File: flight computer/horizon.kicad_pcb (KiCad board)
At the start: 4 copper layers, 50.8 x 95.7 mm, 46 parts, among them J10 Conn_01x02_Pin, J11 USB_C_Receptacle_USB2.0_16P, J12 Conn_01x04, J13 1x3 servo, J14 1x3 servo, J15 arming terminal, J16 arming terminal, J18 Conn_02x03_Counter_Clockwise, J19 Screw_Terminal_01x02, J20 Screw_Terminal_01x02, J21 Conn_02x03_Counter_Clockwise, J5 Screw_Term, J6 1x3 servo, J9 1x3 servo, Q2 DMG2301L, U1 MMCU, U13 LTC4412xS6, U15 AP2112K-3.3, U3 TPS61200DRC, U9 TPS82130

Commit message: chips yummy
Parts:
- added C10: 12pF, Capacitor_SMD:C_0603_1608Metric, B.Cu at (184.1, 55.8)
- added C11: 100nF, Capacitor_SMD:C_0603_1608Metric, F.Cu at (317.2, 42.3)
- added C12: 1uF, Capacitor_SMD:C_0603_1608Metric, F.Cu at (317.2, 44.9)
- added C13: 100nF, Capacitor_SMD:C_0603_1608Metric, F.Cu at (317.2, 47.4)
- added C16: 4n7, Capacitor_SMD:C_0603_1608Metric, F.Cu at (157.7, 28.9)
- added C17: 12pF, Capacitor_SMD:C_0603_1608Metric, B.Cu at (188.0, 52.5)
- added C27: 100n, Capacitor_SMD:C_0603_1608Metric, F.Cu at (157.7, 31.4)
- added C5: 100nF, Capacitor_SMD:C_0603_1608Metric, B.Cu at (186.7, 40.1)
- added C6: 100nF, Capacitor_SMD:C_0603_1608Metric, B.Cu at (185.4, 51.9)
- added C63: 1uF, Capacitor_SMD:C_0603_1608Metric, B.Cu at (187.3, 65.0)
- added C64: 0.1uF, Capacitor_SMD:C_0603_1608Metric, B.Cu at (189.4, 67.1)
- added C65: 0.1uF, Capacitor_SMD:C_0603_1608Metric, B.Cu at (185.9, 63.4)
- added C66: 0.1uF, Capacitor_SMD:C_0603_1608Metric, B.Cu at (184.8, 62.4)
- added C67: 4.7uF, Capacitor_SMD:C_0603_1608Metric, B.Cu at (188.4, 66.0)
- added C7: 100nF, Capacitor_SMD:C_0603_1608Metric, B.Cu at (176.8, 49.2)
- added C72: 1uF, Capacitor_SMD:C_0603_1608Metric, B.Cu at (177.9, 50.3)
- added C77: 100nF, Capacitor_SMD:C_0603_1608Metric, B.Cu at (177.9, 40.4)
- added C78: 100nF, Capacitor_SMD:C_0603_1608Metric, F.Cu at (321.2, 47.4)
- added C79: 100nF, Capacitor_SMD:C_0603_1608Metric, B.Cu at (176.9, 41.4)
- added C8: 100nF, Capacitor_SMD:C_0603_1608Metric, F.Cu at (317.2, 34.8)
- added C9: 100nF, Capacitor_SMD:C_0603_1608Metric, F.Cu at (317.2, 37.3)
- added D7: LED, LED_SMD:LED_0603_1608Metric, F.Cu at (161.8, 28.9)
- added R10: 2.2k, Resistor_SMD:R_0603_1608Metric, B.Cu at (176.4, 58.0)
- added R13: 2.2k, Resistor_SMD:R_0603_1608Metric, B.Cu at (176.4, 60.5)
- added R14: 1.5k, Resistor_SMD:R_0603_1608Metric, F.Cu at (329.3, 27.3)
- added R20: 5k1, Resistor_SMD:R_0603_1608Metric, B.Cu at (198.5, 33.5)
- added R21: 5k1, Resistor_SMD:R_0603_1608Metric, B.Cu at (201.4, 33.5)
- added R22: 330, Resistor_SMD:R_0603_1608Metric, F.Cu at (157.7, 38.9)
- added R26: 2.2K, Resistor_SMD:R_0603_1608Metric, F.Cu at (329.3, 29.8)
- added R29: 2.2K, Resistor_SMD:R_0603_1608Metric, B.Cu at (199.6, 53.5)
- added R30: 2.2K, Resistor_SMD:R_0603_1608Metric, B.Cu at (200.7, 54.6)
- added R6: 4.7k, Resistor_SMD:R_0603_1608Metric, B.Cu at (200.1, 64.0)
- added R7: 4.7k, Resistor_SMD:R_0603_1608Metric, B.Cu at (199.0, 65.1)
- added R9: 1.5k, Resistor_SMD:R_0603_1608Metric, B.Cu at (186.5, 50.8)
- added Y1: Crystal, Crystal:Crystal_AT310_D3.0mm_L10.0mm_Vertical, F.Cu at (187.3, 54.4)
- moved J21 15.3 mm to (192.5, 30.2), turned to 180 degrees
- moved J18 15.1 mm to (206.9, 25.1), turned to 0 degrees
- moved D8 1.83 mm to (199.8, 36.8), turned to -45 degrees
- turned SAMD21G18A-AU1 to -45 degrees
- turned SAMD21G18A-AU2 to -135 degrees
- turned U1 to 45 degrees
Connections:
- J18 pad 2: D+ DMCU-1 -> D+ DMCU-2
- J18 pad 4: unconnected-(J18-Pin_4-Pad4) -> D+ MMCU
- J18 pad 6: D+ DMCU-2 -> D+ DMCU-1
- J21 pad 2: D- DMCU-1 -> D- DMCU-2
- J21 pad 6: D- DMCU-2 -> D- DMCU-1
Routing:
- net I2C0_SDA: track 0.00 -> 24.4 mm, vias 0 -> 2
- net D+: track 0.00 -> 21.4 mm
- net I2C0_SCL: track 0.00 -> 21.4 mm
- net D-: track 0.00 -> 20.3 mm
- net Net-(D26-A): track 0.00 -> 11.0 mm, vias 0 -> 1
- net Net-(U1-XTAL32): track 0.00 -> 4.10 mm
- net Net-(U1-EXTAL32): track 0.00 -> 3.77 mm
- net Net-(J11-CC2): track 0.00 -> 1.84 mm
- net Net-(J11-CC1): track 0.00 -> 1.81 mm
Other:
- board text removed: "WORK ON THIS ONE... the top is a working version of it, so pretty much take our parts, and put them in the some pos if you can, and wire it to the MCU were needed normally. Also, keep it in the same spot as the RF use to be."

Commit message: more wiring fuck this
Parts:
- C11, C12, C13, C78, C8, C9, R14, R26: moved to B.Cu
- moved R14 132.7 mm to (198.4, 49.2), turned to -135 degrees
- moved R26 124.8 mm to (206.5, 52.4), turned to -45 degrees
- moved C9 120.6 mm to (197.0, 47.7), turned to 45 degrees
- moved C12 118.8 mm to (198.5, 41.2), turned to -45 degrees
- moved C8 117.7 mm to (199.6, 40.2), turned to -45 degrees
- moved C78 113.6 mm to (207.9, 39.6), turned to -135 degrees
- moved C13 108.5 mm to (209.0, 40.7), turned to -135 degrees
- moved C11 108.1 mm to (209.4, 49.6), turned to 135 degrees
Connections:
- J18 pad 2: D+ DMCU-2 -> D+ DMCU-1
- J18 pad 6: D+ DMCU-1 -> D+ DMCU-2
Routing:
- net D+ MMCU: track 0.00 -> 48.1 mm
- net D+ DMCU-1: track 0.00 -> 39.2 mm
- net D- MMCU: track 0.00 -> 37.9 mm, vias 0 -> 2
- net D- DMCU-1: track 0.00 -> 28.2 mm
- net D- DMCU-2: track 0.00 -> 23.4 mm, vias 0 -> 2
- net D+ DMCU-2: track 0.00 -> 21.0 mm

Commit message: finished basics, proof check time
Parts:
- C16, C27, D7, R22: moved to B.Cu
- moved C16 46.3 mm to (203.8, 32.8), turned to 180 degrees
- moved C27 46.2 mm to (203.8, 34.4), turned to 180 degrees
- moved R22 46.0 mm to (203.6, 35.9), turned to 180 degrees
- moved D7 45.2 mm to (206.8, 33.5), turned to -120 degrees
- moved R13 17.7 mm to (189.2, 48.2), turned to 0 degrees
- moved R10 15.2 mm to (189.7, 50.6), turned to -30 degrees
- moved C77 0.19 mm to (177.9, 40.2)
- moved C79 0.19 mm to (176.8, 41.3)
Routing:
- net +5V: track 1.91 -> 56.2 mm
- net GND: track 10.8 -> 59.6 mm, vias 9 -> 42
- net SERVO1: track 0.00 -> 43.2 mm, vias 0 -> 1
- net +3.3V: track 3.26 -> 42.2 mm, vias 0 -> 13
- net SERVO2: track 0.00 -> 38.2 mm, vias 0 -> 1
- net CAM_TX: track 0.00 -> 26.6 mm, vias 0 -> 1
- net CAM_RX: track 0.00 -> 24.6 mm, vias 0 -> 1
- net PTD4: track 0.00 -> 23.6 mm, vias 0 -> 2
- net SERVO3: track 0.00 -> 15.5 mm
- net PTA12: track 0.00 -> 15.4 mm, vias 0 -> 2
- net SERVO4: track 0.00 -> 11.0 mm
- net SERVO5: track 0.00 -> 9.93 mm
- net StatusLED_3: track 0.00 -> 5.03 mm, vias 0 -> 1
- net D+ DMCU-1: track 39.2 -> 42.3 mm
- net Net-(D7-A): track 0.00 -> 2.68 mm
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
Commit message: more wiring kms
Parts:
- added D3: LED, LED_SMD:LED_0603_1608Metric, F.Cu at (177.7, 37.0)
- added D4: LED, LED_SMD:LED_0603_1608Metric, F.Cu at (209.7, 36.1)
- added F1: Polyfuse, Fuse:Fuse_0603_1608Metric, F.Cu at (174.4, 32.8)
- added F2: Polyfuse, Fuse:Fuse_0603_1608Metric, F.Cu at (212.8, 30.3)
- added Q1: IRLML6402, Package_TO_SOT_SMD:SOT-23, F.Cu at (143.4, 72.9)
- added Q3: IRLML6402, Package_TO_SOT_SMD:SOT-23, F.Cu at (143.4, 77.5)
- added Q4: IRLML6402, Package_TO_SOT_SMD:SOT-23, F.Cu at (148.3, 72.9)
- added Q5: IRLML6402, Package_TO_SOT_SMD:SOT-23, F.Cu at (148.3, 77.5)
- added Q6: IRLML6402, Package_TO_SOT_SMD:SOT-23, F.Cu at (153.2, 72.9)
- added Q8: IRLML6402, Package_TO_SOT_SMD:SOT-23, F.Cu at (174.4, 35.8)
- added Q9: IRLML6402, Package_TO_SOT_SMD:SOT-23, F.Cu at (212.2, 35.6)
- added R58: 1k, Resistor_SMD:R_0603_1608Metric, F.Cu at (177.2, 38.5)
- added R59: 1k, Resistor_SMD:R_0603_1608Metric, F.Cu at (209.2, 38.3)
- added R62: 100k, Resistor_SMD:R_0603_1608Metric, F.Cu at (159.0, 61.7)
- added R63: 100, Resistor_SMD:R_0603_1608Metric, F.Cu at (159.0, 64.2)
- added R64: 100, Resistor_SMD:R_0603_1608Metric, F.Cu at (159.0, 66.8)
- added R65: 100, Resistor_SMD:R_0603_1608Metric, F.Cu at (159.0, 69.3)
- added R66: 100, Resistor_SMD:R_0603_1608Metric, F.Cu at (163.0, 46.7)
- added R67: 100, Resistor_SMD:R_0603_1608Metric, F.Cu at (163.0, 49.2)
- added R68: 100k, Resistor_SMD:R_0603_1608Metric, F.Cu at (163.0, 51.7)
- added R69: 100k, Resistor_SMD:R_0603_1608Metric, F.Cu at (163.0, 54.2)
- added R70: 100k, Resistor_SMD:R_0603_1608Metric, F.Cu at (163.0, 56.7)
- added R71: 100k, Resistor_SMD:R_0603_1608Metric, F.Cu at (163.0, 59.2)
- added R78: 10k, Resistor_SMD:R_0603_1608Metric, F.Cu at (174.2, 38.5)
- added R79: 100, Resistor_SMD:R_0603_1608Metric, F.Cu at (180.3, 35.4)
- added R80: 10k, Resistor_SMD:R_0603_1608Metric, F.Cu at (212.2, 38.3)
- added R81: 100, Resistor_SMD:R_0603_1608Metric, F.Cu at (212.0, 32.8)
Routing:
- net mosfet2_signalfire: track 0.00 -> 33.9 mm, vias 0 -> 3
- net +5V: track 56.2 -> 79.6 mm
- net mosfet1_signalfire: track 0.00 -> 8.40 mm, vias 0 -> 1
- net Net-(D3-K): track 0.00 -> 6.41 mm
- net Net-(D4-K): track 0.00 -> 6.08 mm
- net Net-(Q8-G): track 0.00 -> 4.33 mm
- net Net-(Q9-D): track 0.00 -> 3.76 mm
- net Net-(Q8-D): track 0.00 -> 3.70 mm
- net GND: track 59.6 -> 63.2 mm, vias 42 -> 43
- net Net-(J20-Pin_1): track 0.00 -> 2.39 mm
- net Net-(SAMD21G18A-AU2-GNDANA): track 0.00 -> 2.01 mm
- net Net-(Q9-G): track 0.00 -> 1.99 mm
- net Net-(J15-Pin_2): track 0.00 -> 1.86 mm
- net Net-(D3-A): track 0.00 -> 1.77 mm

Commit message: wiring fml
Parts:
- removed Q1, Q3, Q4, Q5, Q6: IRLML6402, Package_TO_SOT_SMD:SOT-23
- removed R62, R68, R69, R70, R71: 100k, Resistor_SMD:R_0603_1608Metric
- removed R63, R64, R65, R66, R67: 100, Resistor_SMD:R_0603_1608Metric
- added SW1: CK_KMS2xxG, Button_Switch_SMD:SW_SPST_CK_KMS2xxGP, B.Cu at (169.9, 62.9)
- added U2: MKL02Z32VFG4, Package_DFN_QFN:QFN-16-1EP_3x3mm_P0.5mm_EP1.9x1.9mm, B.Cu at (181.4, 54.0)
- moved C10 0.31 mm to (184.4, 55.7)
- moved Y1 0.11 mm to (187.3, 54.5)
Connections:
- 1x3servo1 pad 2: Net-(1x3servo1-Pin_2) -> +5V
- F2 pad 1: Net-(J20-Pin_1) -> unconnected-(F2-Pad1)
- J13 pad 2: Net-(J13-Pin_2) -> +5V
- J14 pad 2: Net-(J14-Pin_2) -> +5V
- J20 pad 1: Net-(J20-Pin_1) -> unconnected-(J20-Pin_1-Pad1)
- J20 pad 2: Net-(D4-K) -> unconnected-(J20-Pin_2-Pad2)
- J5 pad 1: Net-(IC1-OUT1) -> unconnected-(J5-Pin_1-Pad1)
- J5 pad 2: Net-(IC1-OUT2) -> unconnected-(J5-Pin_2-Pad2)
- J6 pad 2: Net-(J6-Pin_2) -> +5V
- J9 pad 2: Net-(J9-Pin_2) -> +5V
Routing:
- net +5V: track 79.6 -> 121.5 mm
- net nRESET MMCU: track 0.00 -> 27.4 mm, vias 0 -> 2
- net Net-(U2-PTB2/IRQ_7): track 0.00 -> 17.8 mm
- net SWCLK MMCU: track 0.00 -> 16.0 mm, vias 0 -> 4
- net PTA3: track 0.00 -> 15.8 mm, vias 0 -> 2
- net SWDIO MMCU: track 0.00 -> 14.3 mm, vias 0 -> 2
- net PTA2: track 0.00 -> 10.4 mm, vias 0 -> 4
- net GND: track 63.2 -> 68.6 mm, vias 43 -> 47
- net Net-(J20-Pin_1): track 2.39 -> 0.00 mm
- net (no net): track 0.00 -> 2.39 mm
- net +3.3V: track 42.2 -> 43.7 mm, vias 13 -> 14
- net Net-(U1-XTAL32): track 4.10 -> 5.21 mm
- net D+ DMCU-1: track 42.3 -> 41.4 mm, vias 0 -> 2
- net D- MMCU: track 37.9 -> 38.7 mm

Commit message: i did stuffs
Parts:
- added C1: 100 nF, Capacitor_SMD:C_0603_1608Metric, F.Cu at (69.2, 9.72)
- added C14: 8pF, Capacitor_SMD:C_0603_1608Metric, F.Cu at (69.2, 19.8)
- added C15: 100nF, Capacitor_SMD:C_0603_1608Metric, B.Cu at (198.6, 113.0)
- added C18: 4.7uF, Capacitor_SMD:C_0603_1608Metric, F.Cu at (69.2, 24.8)
- added C19: 100nF, Capacitor_SMD:C_0603_1608Metric, F.Cu at (69.2, 27.3)
- added C2: 100 nF, Capacitor_SMD:C_0603_1608Metric, F.Cu at (69.2, 12.2)
- added C20: 100nF, Capacitor_SMD:C_0603_1608Metric, F.Cu at (73.2, 9.72)
- added C3: 100 nF, Capacitor_SMD:C_0603_1608Metric, F.Cu at (69.2, 14.7)
- added C37: 100nF, Capacitor_SMD:C_0603_1608Metric, F.Cu at (73.2, 12.2)
- added C38: 100nF, Capacitor_SMD:C_0603_1608Metric, F.Cu at (73.2, 14.7)
- added C39: 8pF, Capacitor_SMD:C_0603_1608Metric, F.Cu at (73.2, 17.3)
- added C4: 1.2 pF, Capacitor_SMD:C_0603_1608Metric, F.Cu at (69.2, 17.3)
- added C40: 470nF, Capacitor_SMD:C_0603_1608Metric, F.Cu at (73.2, 19.8)
- added C44: 100nF, Capacitor_SMD:C_0603_1608Metric, F.Cu at (73.2, 22.3)
- added C45: 100nF, Capacitor_SMD:C_0603_1608Metric, F.Cu at (73.2, 24.8)
- added C46: 1nF, Capacitor_SMD:C_0603_1608Metric, F.Cu at (73.2, 27.3)
- added C47: 47nF, Capacitor_SMD:C_0603_1608Metric, F.Cu at (77.2, 9.72)
- added C48: 47pF, Capacitor_SMD:C_0603_1608Metric, F.Cu at (77.2, 12.2)
- added C49: 100pF, Capacitor_SMD:C_0603_1608Metric, F.Cu at (77.2, 14.7)
- added C50: 100nF, Capacitor_SMD:C_0603_1608Metric, F.Cu at (77.2, 17.3)
- added C51: 100nF, Capacitor_SMD:C_0603_1608Metric, F.Cu at (77.2, 19.8)
- added D1: D_Schottky, Diode_SMD:D_0603_1608Metric, F.Cu at (102.1, 36.7)
- added D2: PESD5V‑S5ULC, Diode_SMD:D_0603_1608Metric, F.Cu at (102.1, 39.3)
- added FL1: 0900FM15K0039, RF_Converter:Balun_Johanson_0900FM15K0039, F.Cu at (105.9, 37.6)
- added J1: Micro_SD_Card_Det1, Connector_Card:microSD_HC_Hirose_DM3D-SF, F.Cu at (174.5, 111.5)
- added J17: H9161TR-ND, U.FL-R-SMT_01_:HRS_U.FL-R-SMT_01_, F.Cu at (84.9, 40.8)
- added J2: Conn_02x03_Counter_Clockwise, Connector_PinHeader_2.54mm:PinHeader_2x03_P2.54mm_Vertical, F.Cu at (112.1, 10.8)
- added J3: H9161TR-ND, U.FL-R-SMT_01_:HRS_U.FL-R-SMT_01_, F.Cu at (84.9, 30.7)
- added J4: H9161TR-ND, U.FL-R-SMT_01_:HRS_U.FL-R-SMT_01_, F.Cu at (84.9, 35.7)
- added J7: Conn_02x03_Counter_Clockwise, Connector_PinHeader_2.54mm:PinHeader_2x03_P2.54mm_Vertical, F.Cu at (119.3, 10.8)
- added J8: Conn_02x03_Counter_Clockwise, Connector_PinHeader_2.54mm:PinHeader_2x03_P2.54mm_Vertical, F.Cu at (126.5, 10.8)
- added L1: 47 nH, Inductor_SMD:L_0603_1608Metric, F.Cu at (77.2, 22.3)
- added L10: 47nH, Inductor_SMD:L_0603_1608Metric, F.Cu at (77.2, 27.3)
- added L11: 15uH, Inductor_SMD:L_0805_2012Metric, F.Cu at (102.4, 46.6)
- added L3: 3.9 nH, Inductor_SMD:L_0603_1608Metric, F.Cu at (77.2, 24.8)
- added Q7: BSS138, Package_TO_SOT_SMD:SOT-23, F.Cu at (102.5, 43.0)
- added R1: 10 kΩ, Resistor_SMD:R_0603_1608Metric, F.Cu at (81.3, 9.72)
- added R11: 10kΩ, Resistor_SMD:R_0603_1608Metric, F.Cu at (81.3, 17.3)
- added R12: 10kΩ, Resistor_SMD:R_0603_1608Metric, B.Cu at (176.0, 106.1)
- added R2: 10 kΩ, Resistor_SMD:R_0603_1608Metric, F.Cu at (81.3, 12.2)
- added R27: 10k, Resistor_SMD:R_0603_1608Metric, F.Cu at (81.3, 22.3)
- added R3: 10k, Resistor_SMD:R_0603_1608Metric, F.Cu at (111.8, 19.4)
- added R37: 10k, Resistor_SMD:R_0603_1608Metric, F.Cu at (81.3, 24.8)
- added R38: 10k, Resistor_SMD:R_0603_1608Metric, F.Cu at (81.3, 27.3)
- added R39: 10k, Resistor_SMD:R_0603_1608Metric, F.Cu at (85.3, 9.72)
- added R4: 10k, Resistor_SMD:R_0603_1608Metric, F.Cu at (111.8, 21.9)
- added R5: 10k, Resistor_SMD:R_0603_1608Metric, F.Cu at (111.8, 24.4)
- added R52: 10k, Resistor_SMD:R_0603_1608Metric, F.Cu at (85.3, 12.2)
- added R53: 10k, Resistor_SMD:R_0603_1608Metric, F.Cu at (85.3, 14.7)
- added R54: 10kΩ, Resistor_SMD:R_0603_1608Metric, B.Cu at (173.1, 117.0)
- added R55: 10kΩ, Resistor_SMD:R_0603_1608Metric, B.Cu at (170.6, 115.3)
- added R56: 10k, Resistor_SMD:R_0603_1608Metric, F.Cu at (179.3, 103.8)
- added R72: 2k2, Resistor_SMD:R_0603_1608Metric, F.Cu at (85.3, 24.8)
- added R8: 100, Resistor_SMD:R_0603_1608Metric, F.Cu at (81.3, 14.7)
- added R87: 220, Resistor_SMD:R_0603_1608Metric, F.Cu at (85.3, 27.3)
- added R88: 220, Resistor_SMD:R_0603_1608Metric, F.Cu at (89.3, 9.72)
- added R89: 220, Resistor_SMD:R_0603_1608Metric, F.Cu at (89.3, 12.2)
- added R90: 220, Resistor_SMD:R_0603_1608Metric, F.Cu at (89.3, 14.7)
- added R91: 220, Resistor_SMD:R_0603_1608Metric, F.Cu at (89.3, 17.3)
- added R92: 220, Resistor_SMD:R_0603_1608Metric, F.Cu at (89.3, 19.8)
- added R93: 220, Resistor_SMD:R_0603_1608Metric, F.Cu at (89.3, 22.3)
- added R94: 220, Resistor_SMD:R_0603_1608Metric, F.Cu at (89.3, 24.8)
- added R95: 220, Resistor_SMD:R_0603_1608Metric, F.Cu at (89.3, 27.3)
- added R96: 220, Resistor_SMD:R_0603_1608Metric, F.Cu at (111.8, 27.0)
- added R97: 220, Resistor_SMD:R_0603_1608Metric, F.Cu at (111.8, 29.5)
- added R98: 220, Resistor_SMD:R_0603_1608Metric, F.Cu at (111.8, 32.0)
- added U10: LSM6DS3, Package_LGA:LGA-14_3x2.5mm_P0.5mm_LayoutBorder3x4y, F.Cu at (90.0, 45.2)
- added U16: SX1262IMLTRT, Package_DFN_QFN:QFN-24-1EP_4x4mm_P0.5mm_EP2.6x2.6mm, F.Cu at (97.0, 38.5)
- added U17: PE4259, Package_TO_SOT_SMD:SOT-363_SC-70-6, F.Cu at (84.2, 45.7)
- added U5: LPS22HB, Package_LGA:ST_HLGA-10_2x2mm_P0.5mm_LayoutBorder3x2y, F.Cu at (106.0, 30.4)
- added U6: GPS, RF_GPS:Quectel_L96, F.Cu at (74.6, 38.2)
- added U8: NAND, Package_SO:SOIC-8_5.3x5.3mm_P1.27mm, B.Cu at (174.5, 111.5)
- added Y2: 32MHz, Crystal:Crystal_SMD_3225-4Pin_3.2x2.5mm, F.Cu at (96.5, 43.9)
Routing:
- net NAND_MOSI MMCU: track 0.00 -> 17.1 mm, vias 0 -> 1
- net CS_SD MMCU: track 1.76 -> 13.9 mm, vias 0 -> 1
- net NAND_MISO MMCU: track 0.00 -> 9.17 mm, vias 0 -> 1
- net SPI0_SCK MMCU: track 0.00 -> 8.93 mm, vias 0 -> 1
- net +3.3V: track 43.7 -> 51.4 mm, vias 14 -> 18
- net CS_NAND MMCU: track 2.23 -> 6.13 mm
- net GND: track 68.6 -> 72.0 mm, vias 47 -> 50
- net Net-(U8-~{HOLD}/~{RESET}/IO_{3}): track 0.00 -> 1.94 mm
- net Net-(U8-~{WP}/IO_{2}): track 0.00 -> 1.87 mm

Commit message: scooter please wire the stuff thats off the board to the side
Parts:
- removed C44, C45, C50, C51: 100nF, Capacitor_SMD:C_0603_1608Metric
- removed J2, J7, J8: Conn_02x03_Counter_Clockwise, Connector_PinHeader_2.54mm:PinHeader_2x03_P2.54mm_Vertical
- removed R27, R3, R37, R38, R39, R4, R5, R52, R53: 10k, Resistor_SMD:R_0603_1608Metric
- removed R87, R88, R89, R90, R91, R92, R93, R94, R95, R96, R97, R98: 220, Resistor_SMD:R_0603_1608Metric
- removed U10: LSM6DS3, Package_LGA:LGA-14_3x2.5mm_P0.5mm_LayoutBorder3x4y
- removed U5: LPS22HB, Package_LGA:ST_HLGA-10_2x2mm_P0.5mm_LayoutBorder3x2y
- moved C20 176.5 mm to (151.7, 167.9), turned to 90 degrees
- moved R1 166.5 mm to (106.8, 174.3)
- moved R2 166.5 mm to (106.8, 176.8)
- moved C14 164.1 mm to (34.0, 180.1)
- moved C37 164.1 mm to (38.0, 172.5)
- moved C38 164.1 mm to (38.0, 175.1)
- moved C39 164.1 mm to (38.0, 177.6)
- moved C40 164.1 mm to (38.0, 180.1)
- moved C1 163.5 mm to (96.1, 171.0)
- moved C4 163.5 mm to (96.1, 178.5)
- moved C2 163.5 mm to (96.1, 173.5)
- moved C3 163.5 mm to (96.1, 176.0)
- moved C47 158.1 mm to (68.6, 167.5)
- moved C48 158.1 mm to (68.6, 170.1)
- moved C49 158.1 mm to (68.6, 172.6)
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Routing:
- net SPI0_SCK MMCU: track 8.93 -> 19.5 mm
- net SD_DETECT: track 0.00 -> 2.17 mm
- net GND: track 72.0 -> 73.2 mm, vias 50 -> 51

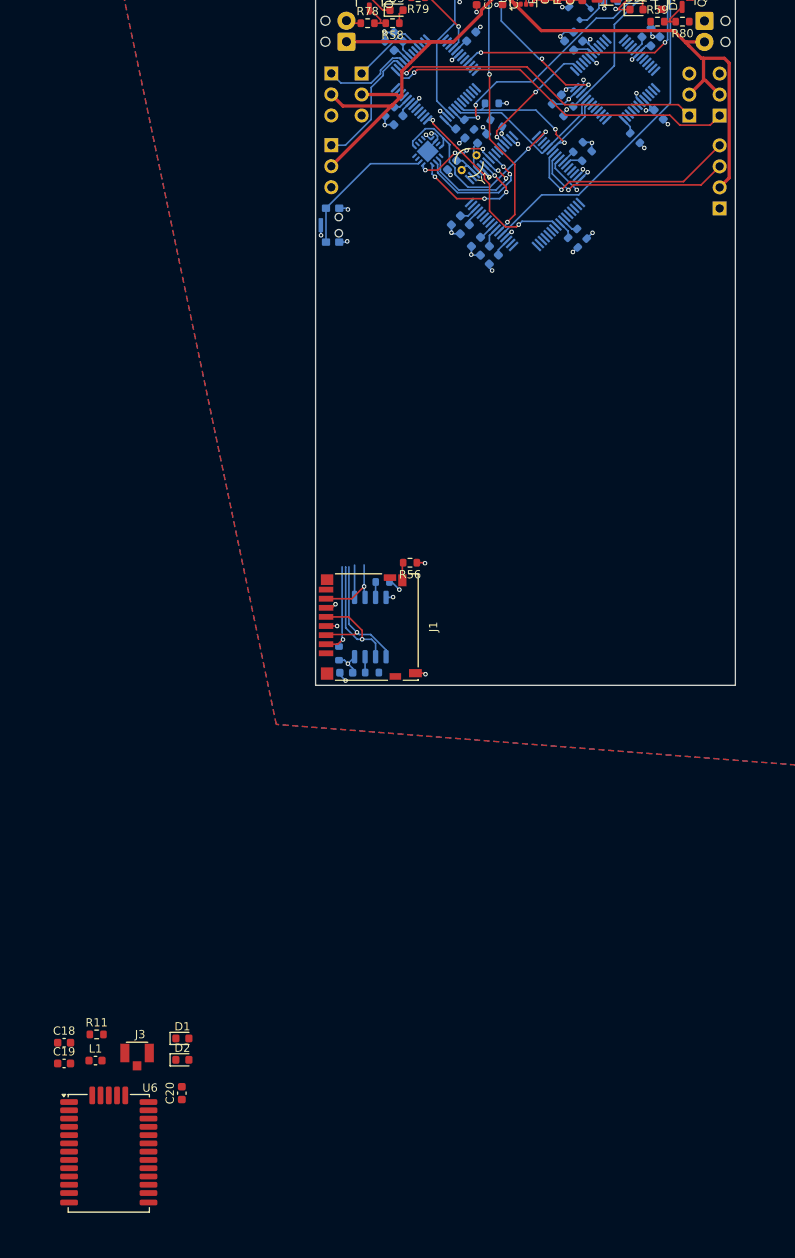
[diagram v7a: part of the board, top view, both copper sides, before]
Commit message: routed GPS for H1
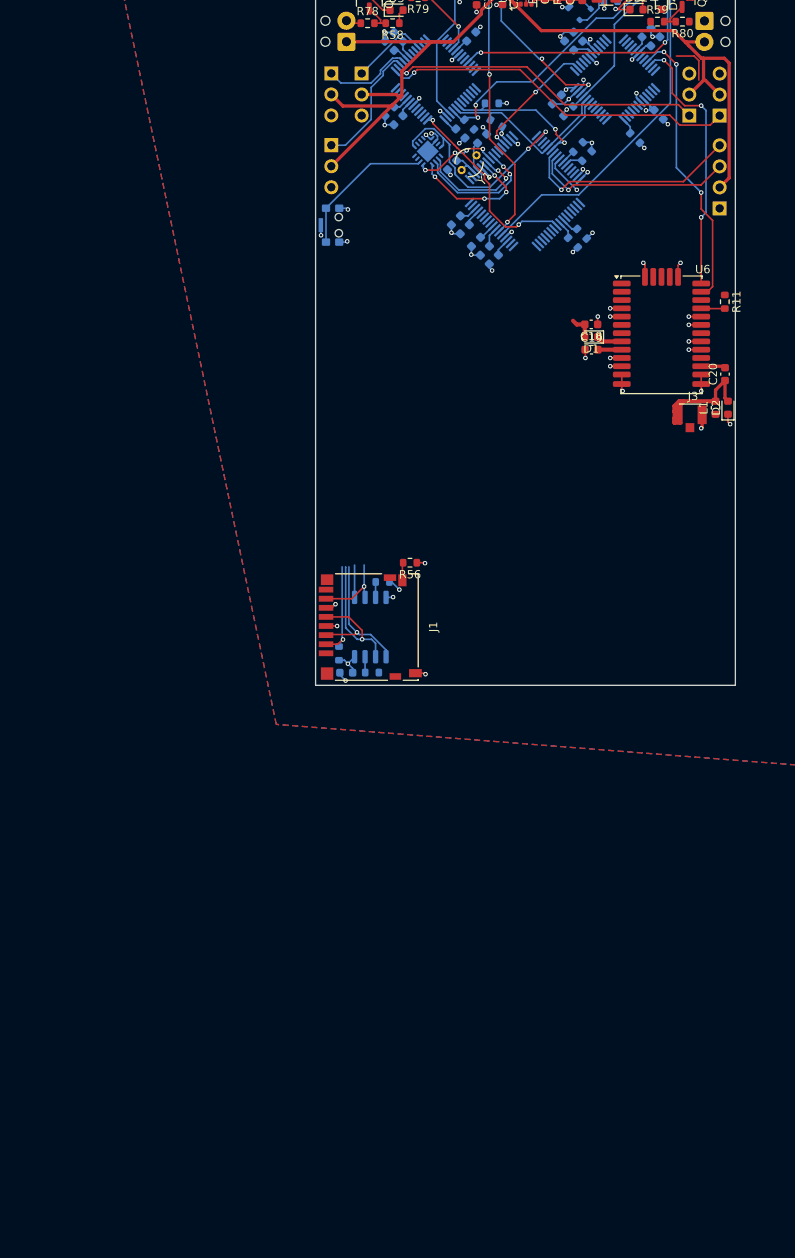
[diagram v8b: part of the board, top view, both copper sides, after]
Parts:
- moved U6 119.4 mm to (209.7, 76.2)
- moved R11 116.7 mm to (217.4, 72.2), turned to -90 degrees
- moved C20 108.9 mm to (217.4, 81.0)
- moved L1 108.8 mm to (216.2, 85.0), turned to 90 degrees
- moved C18 107.7 mm to (201.2, 74.9), turned to 180 degrees
- moved C19 107.3 mm to (201.2, 78.0)
- moved D2 102.8 mm to (217.7, 85.0), turned to 90 degrees
- moved J3 102.1 mm to (213.1, 85.9)
- moved D1 98.2 mm to (201.2, 76.5), turned to 180 degrees
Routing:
- net TX TMCU: track 0.00 -> 35.0 mm, vias 0 -> 3
- net RX TMCU: track 0.00 -> 32.5 mm, vias 0 -> 3
- net GND: track 73.2 -> 97.4 mm, vias 51 -> 67
- net Net-(D2-A): track 0.00 -> 20.4 mm
- net +3.3V: track 51.4 -> 57.4 mm
- net (no net): track 2.39 -> 7.68 mm
- net Net-(D1-K): track 0.00 -> 3.13 mm
- net Net-(U6-RF_OUT): track 0.00 -> 2.95 mm
- net Net-(U6-~{RESET}): track 0.00 -> 2.87 mm
